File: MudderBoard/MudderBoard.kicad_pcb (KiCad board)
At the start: 2 copper layers, 157 parts, among them K1 AZ2850-2A-12DE, M1 NMOS, M2 NMOS, M3 N-MOSFET, M4 N-MOSFET, Q1 CSD16327Q3, Q2 NPN, U1 LM5122QMH/NOPB, U2 TPS566242DRLR, U3 LP38691DTX-3.3/NOPB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

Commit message: edited lidar footprints
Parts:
- moved R20 72.9 mm to (76.4, 82.7)
- moved C17 72.9 mm to (50.0, 85.0)
- moved C18 72.9 mm to (50.0, 88.1)
- moved D4 72.9 mm to (32.8, 83.8)
- moved K1 72.9 mm to (70.2, 45.2)
- moved R18 72.9 mm to (67.8, 78.3)
- moved R19 72.9 mm to (67.8, 81.1)
- moved U5 72.9 mm to (52.1, 80.2)
- moved U6 72.9 mm to (43.5, 80.2)
- moved U7 72.9 mm to (43.5, 86.6)
- moved C19 72.9 mm to (58.6, 78.4)
- moved C20 72.9 mm to (58.6, 81.3)
- moved Q2 72.9 mm to (73.3, 79.2)
- moved R16 72.9 mm to (72.3, 82.6)
- moved R17 72.9 mm to (72.3, 85.1)
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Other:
- board outline added: 248.2 x 122.9 mm

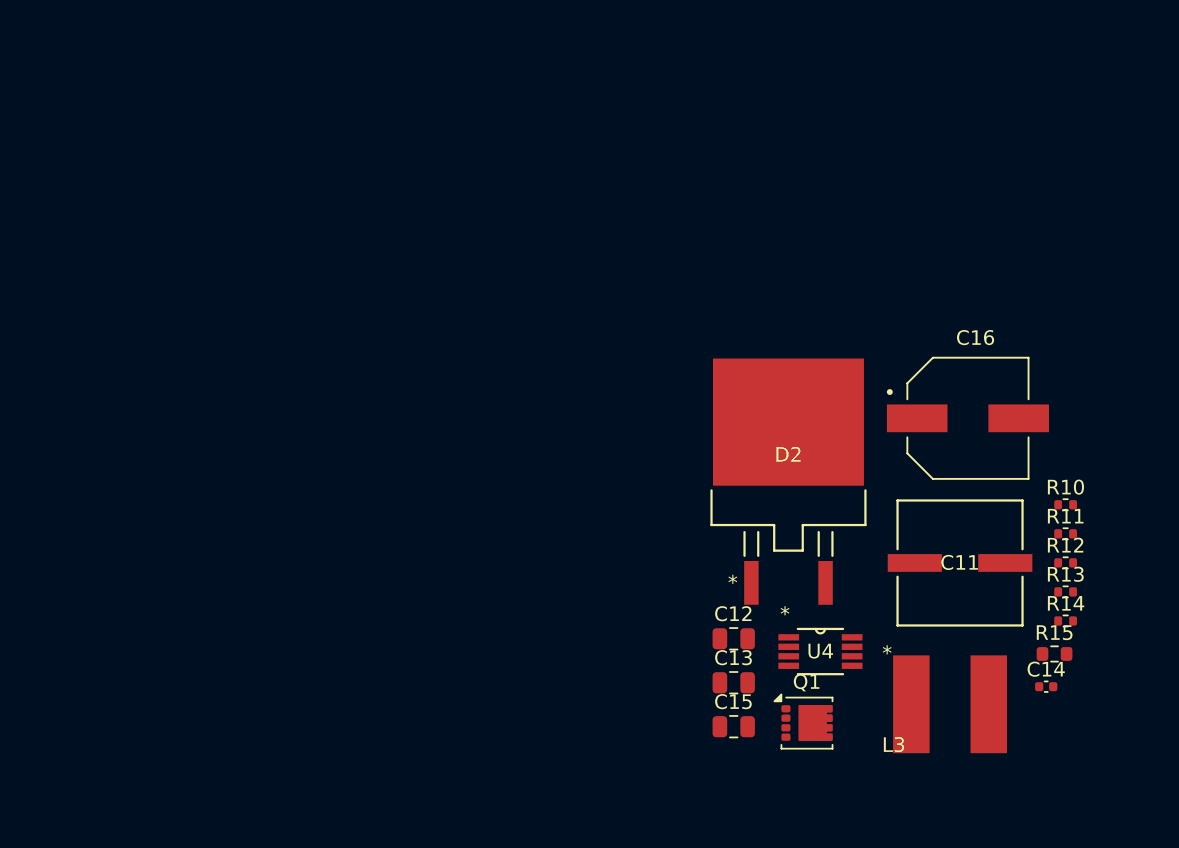
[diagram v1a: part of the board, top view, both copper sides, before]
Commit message: Preliminary layout for jetson portion
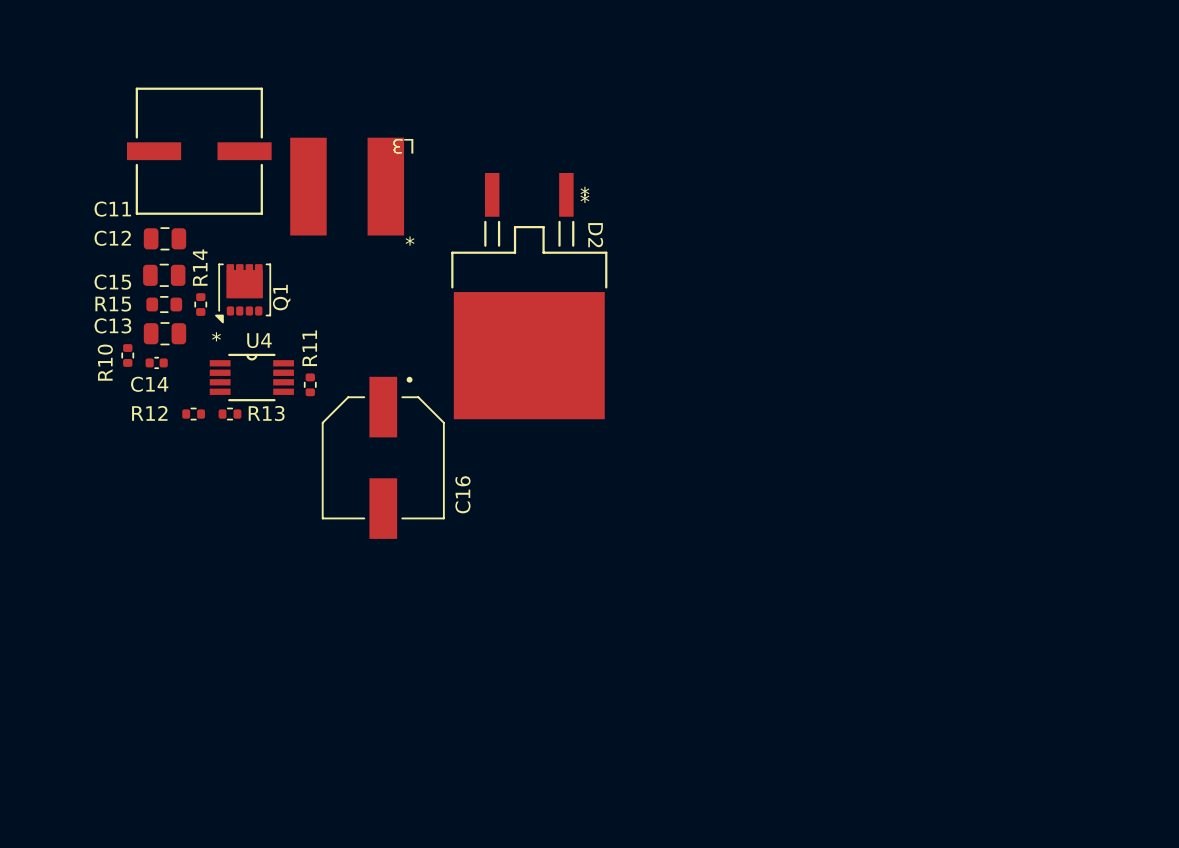
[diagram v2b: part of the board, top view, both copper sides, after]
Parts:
- moved R15 65.5 mm to (155.0, 114.5), turned to 180 degrees
- moved R10 65.0 mm to (152.5, 118.0), turned to 90 degrees
- moved C14 64.8 mm to (154.5, 118.5), turned to 180 degrees
- moved R14 63.1 mm to (157.5, 114.5), turned to 90 degrees
- moved R12 60.6 mm to (157.0, 122.0)
- moved C11 59.2 mm to (157.4, 104.0), turned to 180 degrees
- moved R13 58.5 mm to (159.5, 122.0), turned to 180 degrees
- moved L3 53.8 mm to (171.4, 103.1), turned to 180 degrees
- moved R11 52.7 mm to (165.0, 120.0), turned to -90 degrees
- moved C15 49.8 mm to (155.0, 112.5), turned to 180 degrees
- moved Q1 48.6 mm to (160.5, 113.5), turned to 90 degrees
- moved C12 47.6 mm to (155.1, 110.0), turned to 180 degrees
- moved C13 45.7 mm to (155.1, 116.5), turned to 180 degrees
- moved U4 43.2 mm to (161.0, 119.5)
- moved C16 40.1 mm to (170.0, 125.0), turned to -90 degrees
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
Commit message: lidar preliminary layout
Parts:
- moved R8 44.8 mm to (218.7, 91.7), turned to 180 degrees
- moved C6 42.4 mm to (227.4, 86.5), turned to -90 degrees
- moved C3 40.6 mm to (227.4, 81.6), turned to 90 degrees
- moved C8 36.0 mm to (218.8, 88.4), turned to 90 degrees
- moved C5 35.4 mm to (211.3, 85.0), turned to 180 degrees
- moved R4 35.2 mm to (224.4, 87.1), turned to -90 degrees
- moved C7 33.8 mm to (221.6, 87.5), turned to 180 degrees
- moved R6 32.1 mm to (211.0, 86.8), turned to 180 degrees
- moved R7 31.6 mm to (221.3, 89.2)
- moved L1 31.3 mm to (218.8, 68.9), turned to 90 degrees
- moved C4 30.9 mm to (228.6, 75.7)
- moved R9 30.5 mm to (215.7, 87.7), turned to -90 degrees
- moved D1 30.3 mm to (233.8, 77.8), turned to -90 degrees
- moved R1 30.1 mm to (206.5, 82.0), turned to -90 degrees
- moved R2 29.4 mm to (211.3, 83.2), turned to 180 degrees
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
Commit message: PWM-DC prelim layout
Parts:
- moved K1 87.2 mm to (90.8, -39.6), turned to -90 degrees
- moved D4 49.1 mm to (62.5, 44.8)
- moved R17 46.5 mm to (32.7, 60.8)
- moved R16 40.7 mm to (32.7, 73.3)
- moved C20 33.3 mm to (79.9, 55.7)
- moved R23 33.3 mm to (84.3, 55.7)
- moved C18 29.3 mm to (33.5, 63.9), turned to -90 degrees
- moved U7 26.6 mm to (40.7, 60.1)
- moved R20 24.4 mm to (65.1, 61.0)
- moved Q2 22.8 mm to (66.8, 57.2)
- moved C17 22.2 mm to (33.5, 70.2), turned to 90 degrees
- moved U5 19.5 mm to (65.8, 66.4)
- moved R22 17.2 mm to (59.2, 61.6), turned to 90 degrees
- moved R18 16.4 mm to (75.3, 63.8), turned to 90 degrees
- moved R19 14.5 mm to (75.3, 68.7), turned to 90 degrees
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
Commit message: pixhawk layout prelim
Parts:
- moved Rfbt1 38.1 mm to (175.3, 42.1), turned to 180 degrees
- moved U2 28.9 mm to (167.8, 46.0)
- moved Cout1 28.5 mm to (164.6, 51.6)
- moved Cout2 28.4 mm to (164.6, 54.2)
- moved Cout3 28.3 mm to (164.6, 56.9)
- moved Cout4 28.1 mm to (164.6, 59.6)
- moved Cin2 18.0 mm to (166.8, 39.7)
- moved Cin1 17.5 mm to (166.8, 37.4)
- moved Rfbb1 17.0 mm to (170.8, 42.1), turned to -90 degrees
- moved Cinx1 15.7 mm to (166.8, 42.1)
- moved L2 14.0 mm to (158.4, 47.5), turned to -90 degrees
- moved Coutx1 13.8 mm to (164.6, 49.2)
- moved Cff1 5.79 mm to (145.5, 48.9)
- moved CinLDO1 5.79 mm to (145.5, 37.6)
- moved CoLDO1 5.79 mm to (145.5, 42.6)
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
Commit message: test
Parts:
- moved Rent1 23.4 mm to (163.2, 37.9), turned to -90 degrees
- moved Renb1 20.8 mm to (163.2, 40.1), turned to -90 degrees
- moved CinLDO1 13.3 mm to (142.4, 50.5), turned to 180 degrees
- moved CoLDO1 11.5 mm to (137.2, 50.6)
- moved Cff1 4.50 mm to (143.6, 53.0)

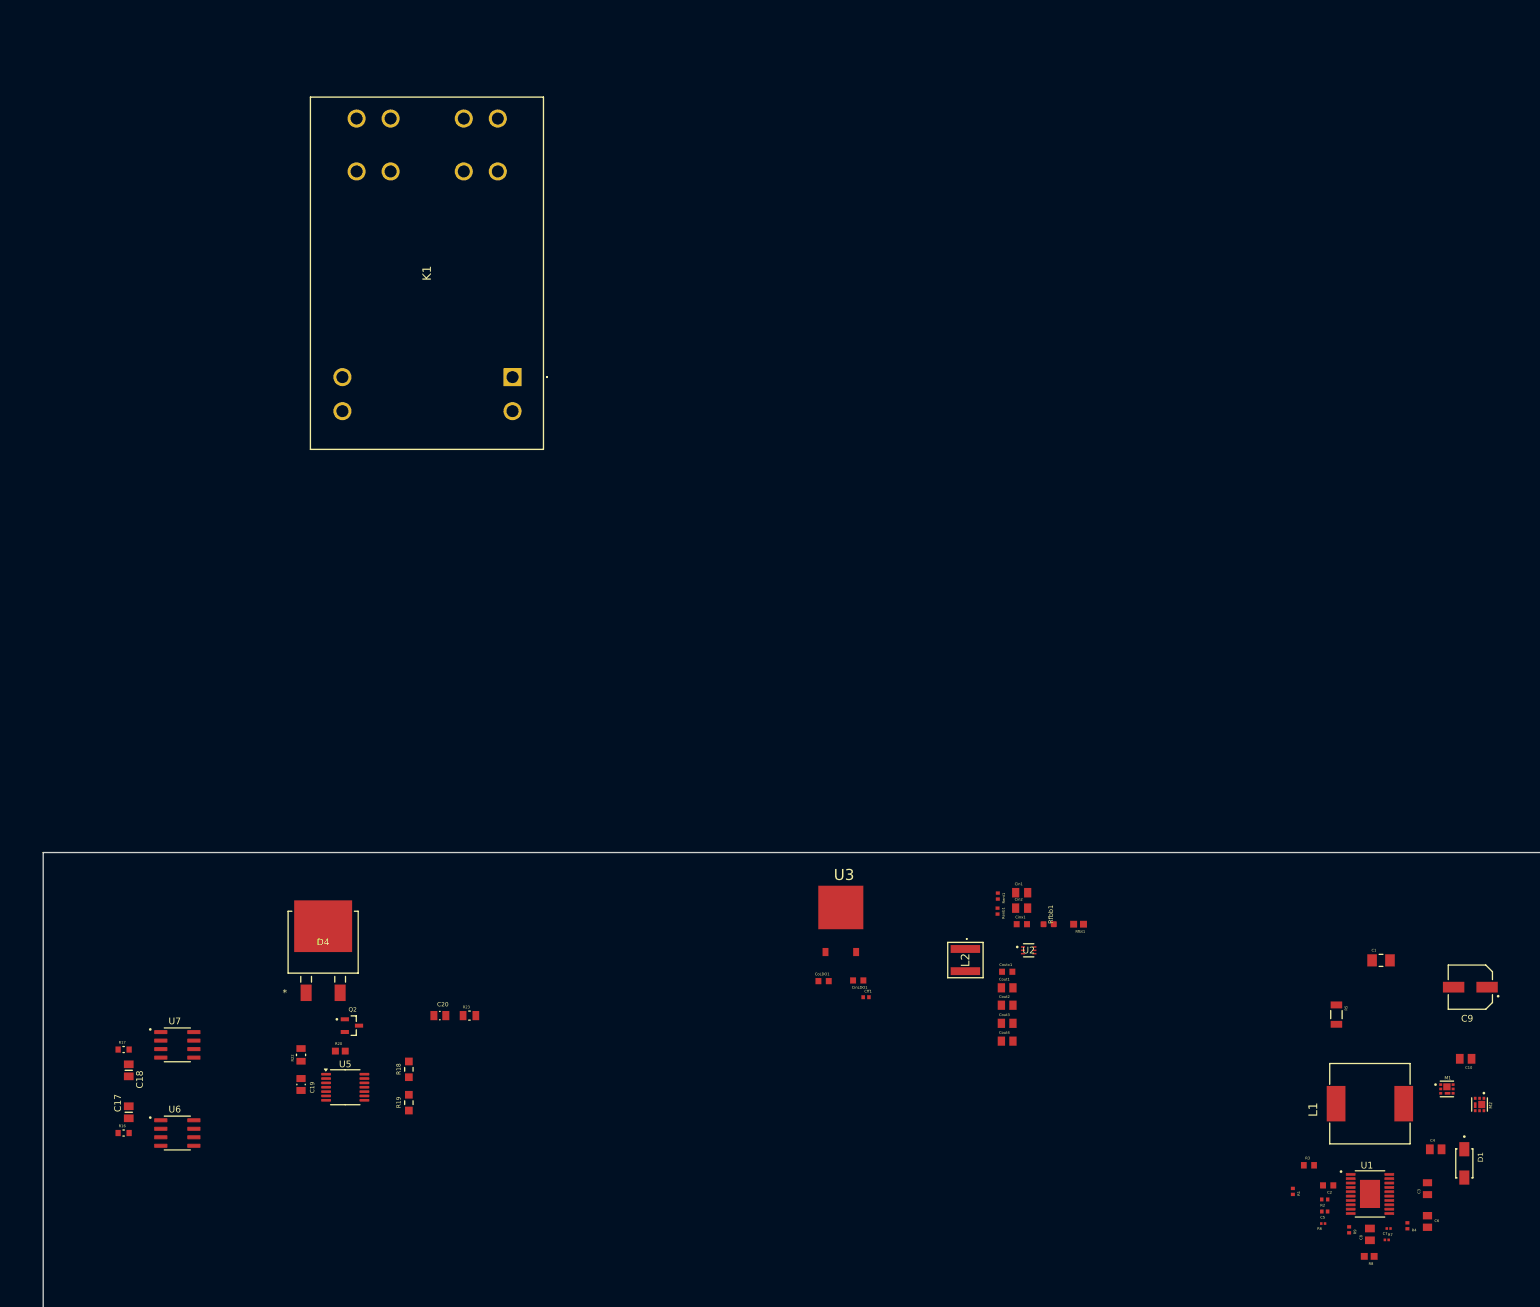
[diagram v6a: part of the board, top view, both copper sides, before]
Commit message: Layout
Pixhawk and Lidar
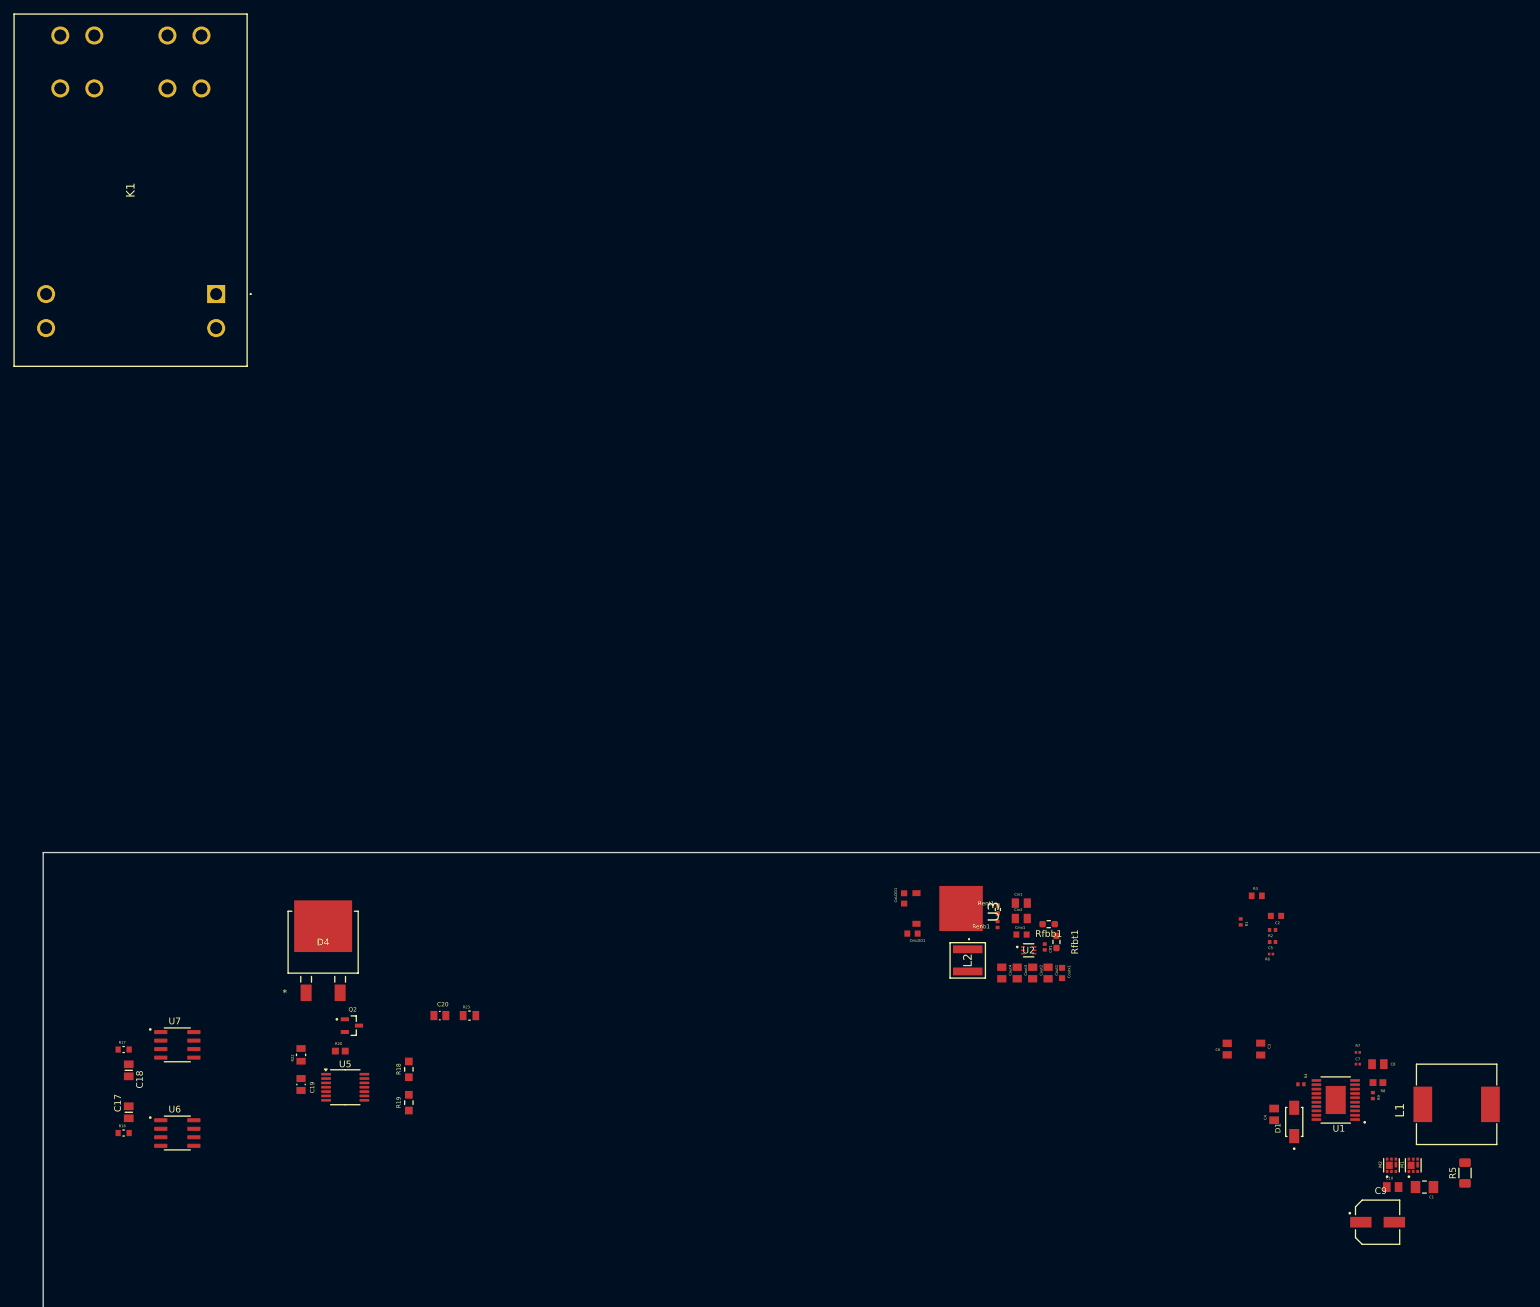
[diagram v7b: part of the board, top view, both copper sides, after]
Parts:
- R5: footprint Lidar_Foot:RESC3015X65N -> Resistor_SMD:R_1206_3216Metric_Pad1.30x1.75mm_HandSolder
- Renb1: value 14K3 -> 14k3
- Rent1: value 100K -> 100k; footprint PH_Foot:RESC1005X40N -> Resistor_SMD:R_0402_1005Metric_Pad0.72x0.64mm_HandSolder
- Rfbb1: value 30K -> 30k; footprint PH_Foot:R0603 -> Resistor_SMD:R_0603_1608Metric_Pad0.98x0.95mm_HandSolder
- Rfbt1: value 220K -> 220k; footprint PH_Foot:RESC1607X60N -> Resistor_SMD:R_0603_1608Metric_Pad0.98x0.95mm_HandSolder
- moved K1 46.0 mm to (46.5, -52.0)
- moved C5 41.0 mm to (204.3, 44.8)
- moved R1 41.0 mm to (199.5, 41.8)
- moved R2 41.0 mm to (204.3, 43.0)
- moved C2 41.0 mm to (204.8, 40.9)
- moved R3 41.0 mm to (201.9, 37.9)
- moved R6 41.0 mm to (204.0, 46.6)
- moved C6 39.5 mm to (197.5, 60.8), turned to 90 degrees
- moved C9 37.7 mm to (219.9, 86.6), turned to 0 degrees
- moved C1 34.5 mm to (226.9, 81.3), turned to 180 degrees
- moved C3 32.5 mm to (202.5, 60.8), turned to -90 degrees
- moved R5 30.5 mm to (233.0, 79.2), turned to 90 degrees
- moved R7 28.3 mm to (217.0, 61.2), turned to 180 degrees
- moved Cff1 27.7 mm to (170.2, 45.5), turned to -90 degrees
- moved R4 26.4 mm to (208.5, 66.0), turned to 180 degrees
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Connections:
- C19 pad 1: /PWM-DC/THRUST_SIG -> AGND
- C19 pad 2: AGND -> /PWM-DC/THRUST_SIG
- Cin1 pad 2: GND1 -> AGND
- Cin2 pad 2: GND1 -> AGND
- CinLDO1 pad 2: GND1 -> AGND
- Cinx1 pad 2: GND1 -> AGND
- CoLDO1 pad 2: GND1 -> AGND
- Cout1 pad 2: GND1 -> AGND
- Cout2 pad 2: GND1 -> AGND
- Cout3 pad 2: GND1 -> AGND
- Cout4 pad 2: GND1 -> AGND
- Coutx1 pad 2: GND1 -> AGND
- Renb1 pad 2: GND1 -> AGND
- Rfbb1 pad 2: GND1 -> AGND
- U2 pad 3: GND1 -> AGND
- U2 pad 4: GND1 -> AGND
- U3 pad 2: GND1 -> AGND
